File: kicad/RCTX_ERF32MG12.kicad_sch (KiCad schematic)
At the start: 98 parts, among them J20 BUZZER, J21 USB_OTG, P1 SD Card, P2 Nokia 5110 display, Q1 Q_PMOS_DGS, SW1 RESET, U1 PIC16(L)F1459-I_ML

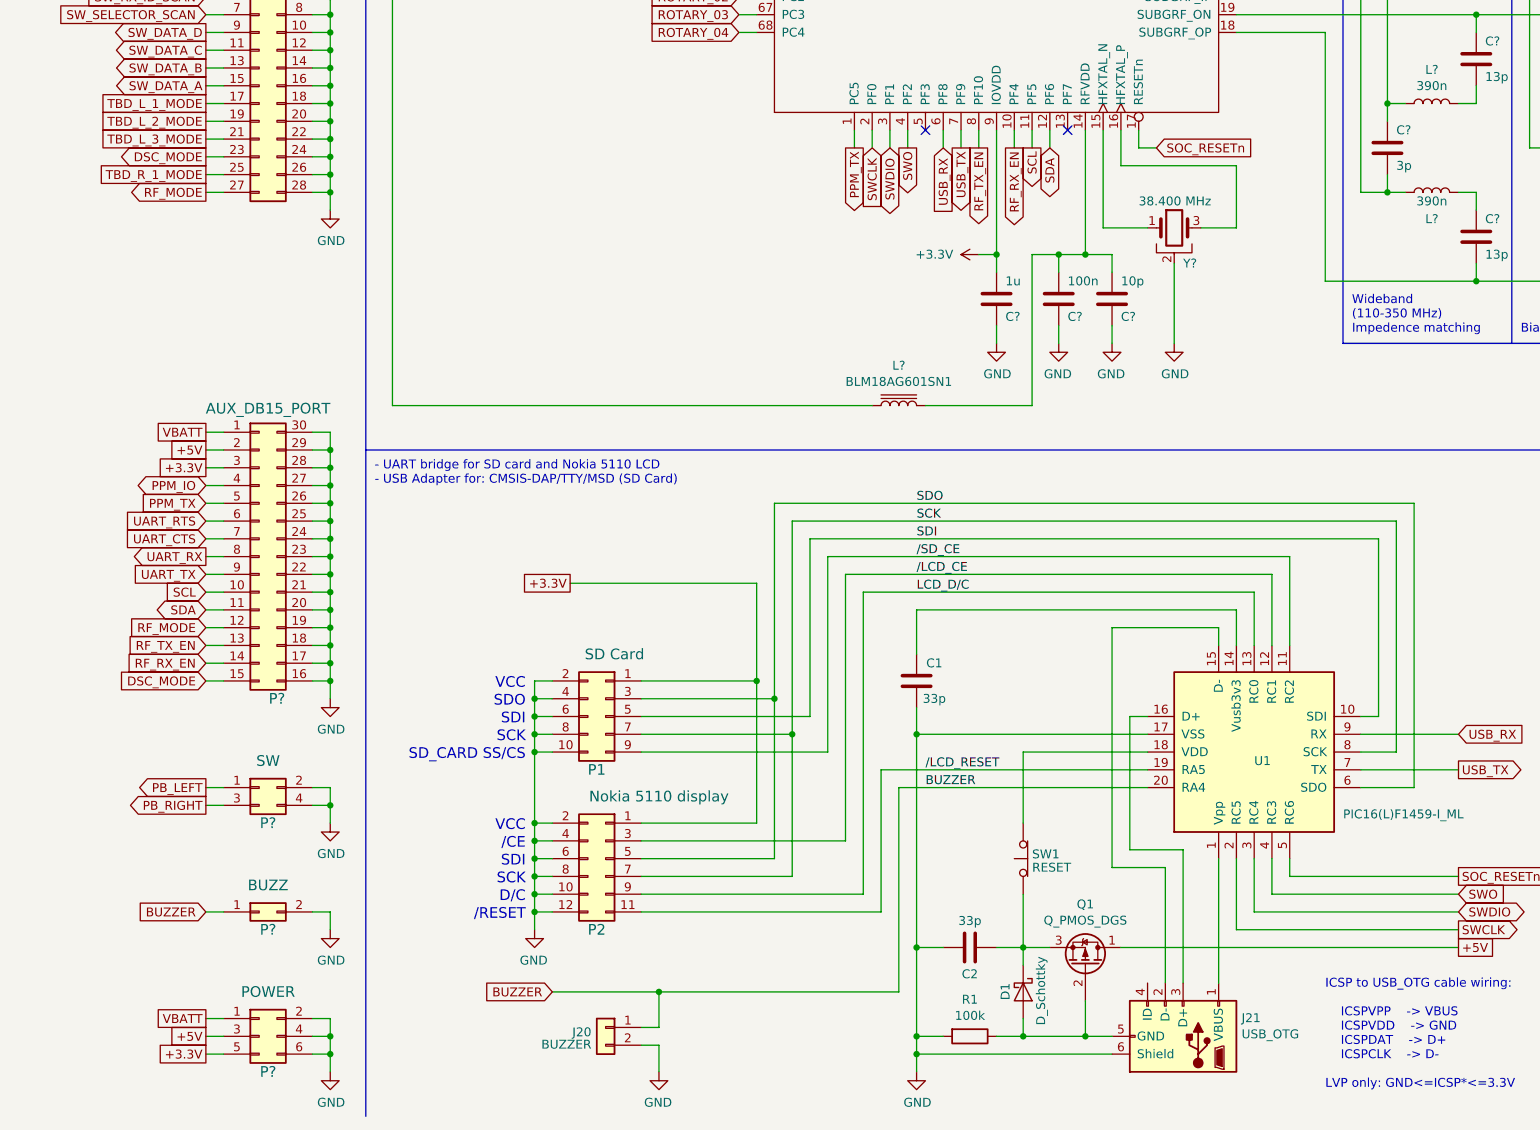
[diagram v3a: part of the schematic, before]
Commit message: Changing the buzzer connector
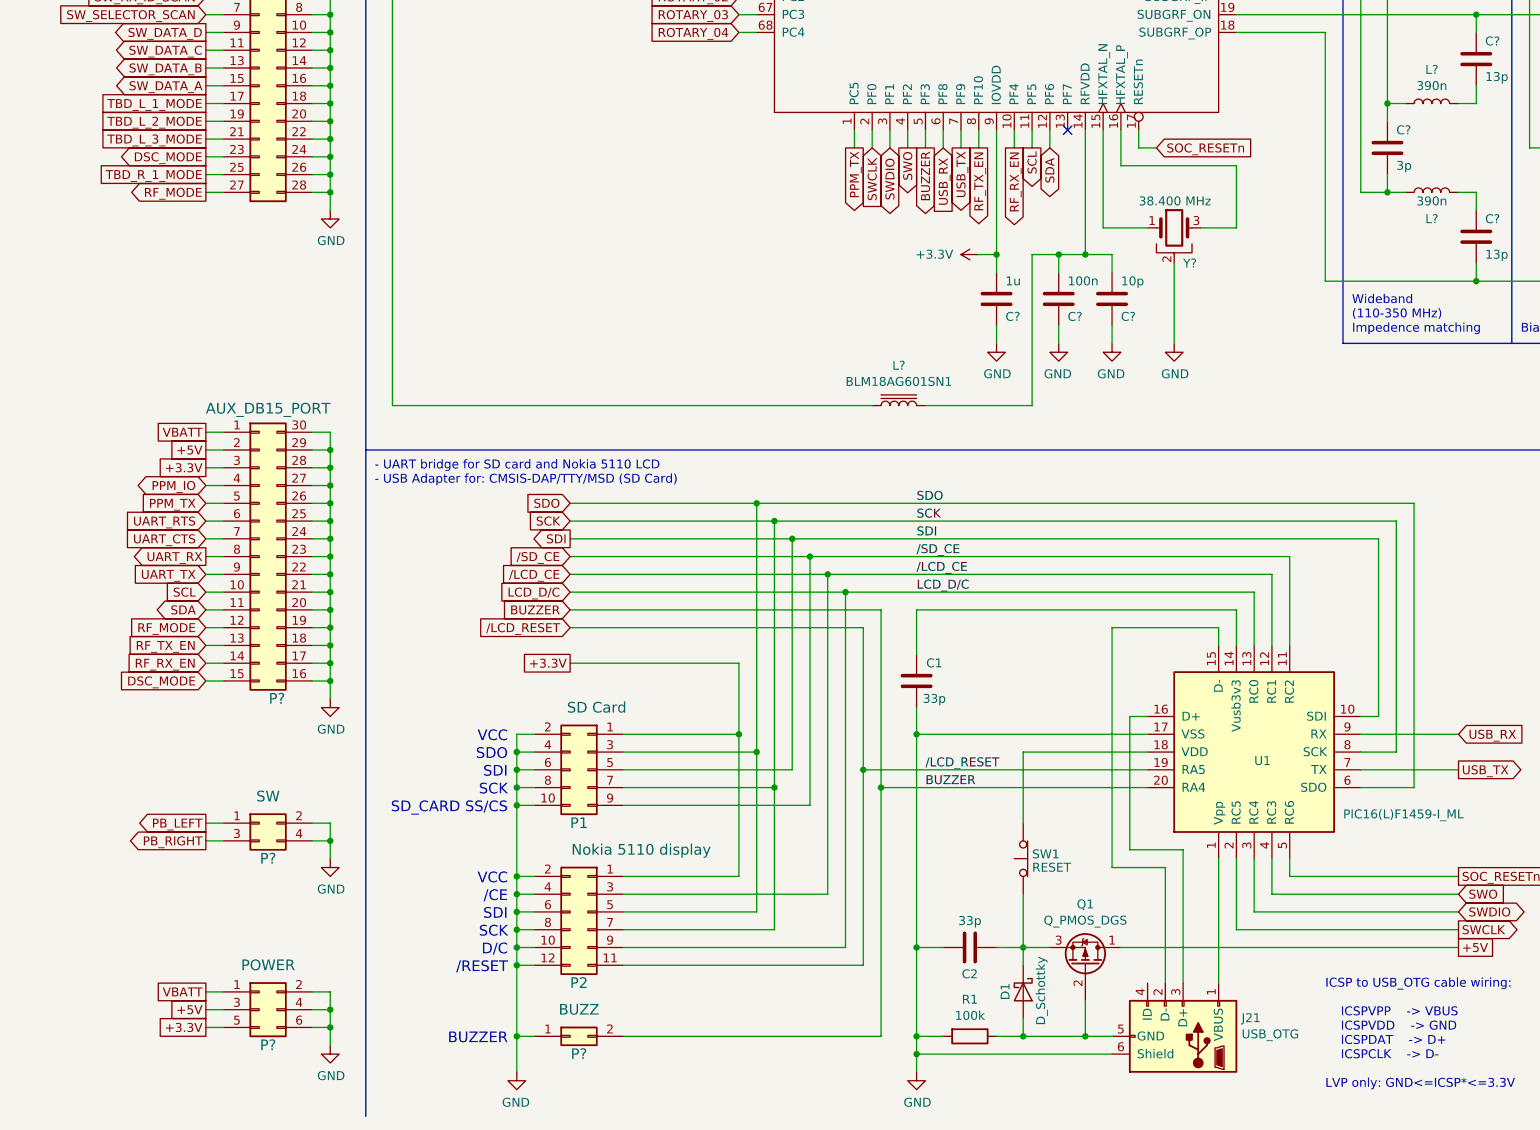
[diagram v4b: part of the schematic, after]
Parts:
- removed J20: BUZZER, symbol Connector_Generic:Conn_01x02
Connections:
- net BUZZER: now also P?.2 (Pin_2), U?.5 (PF3); no longer P?.1 (Pin_1)
- net GND: now also P?.1 (Pin_1); no longer P?.2 (Pin_2)
- no-connect marks 3 -> 2
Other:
- note added: "BUZZER"
- moved on the sheet: P?

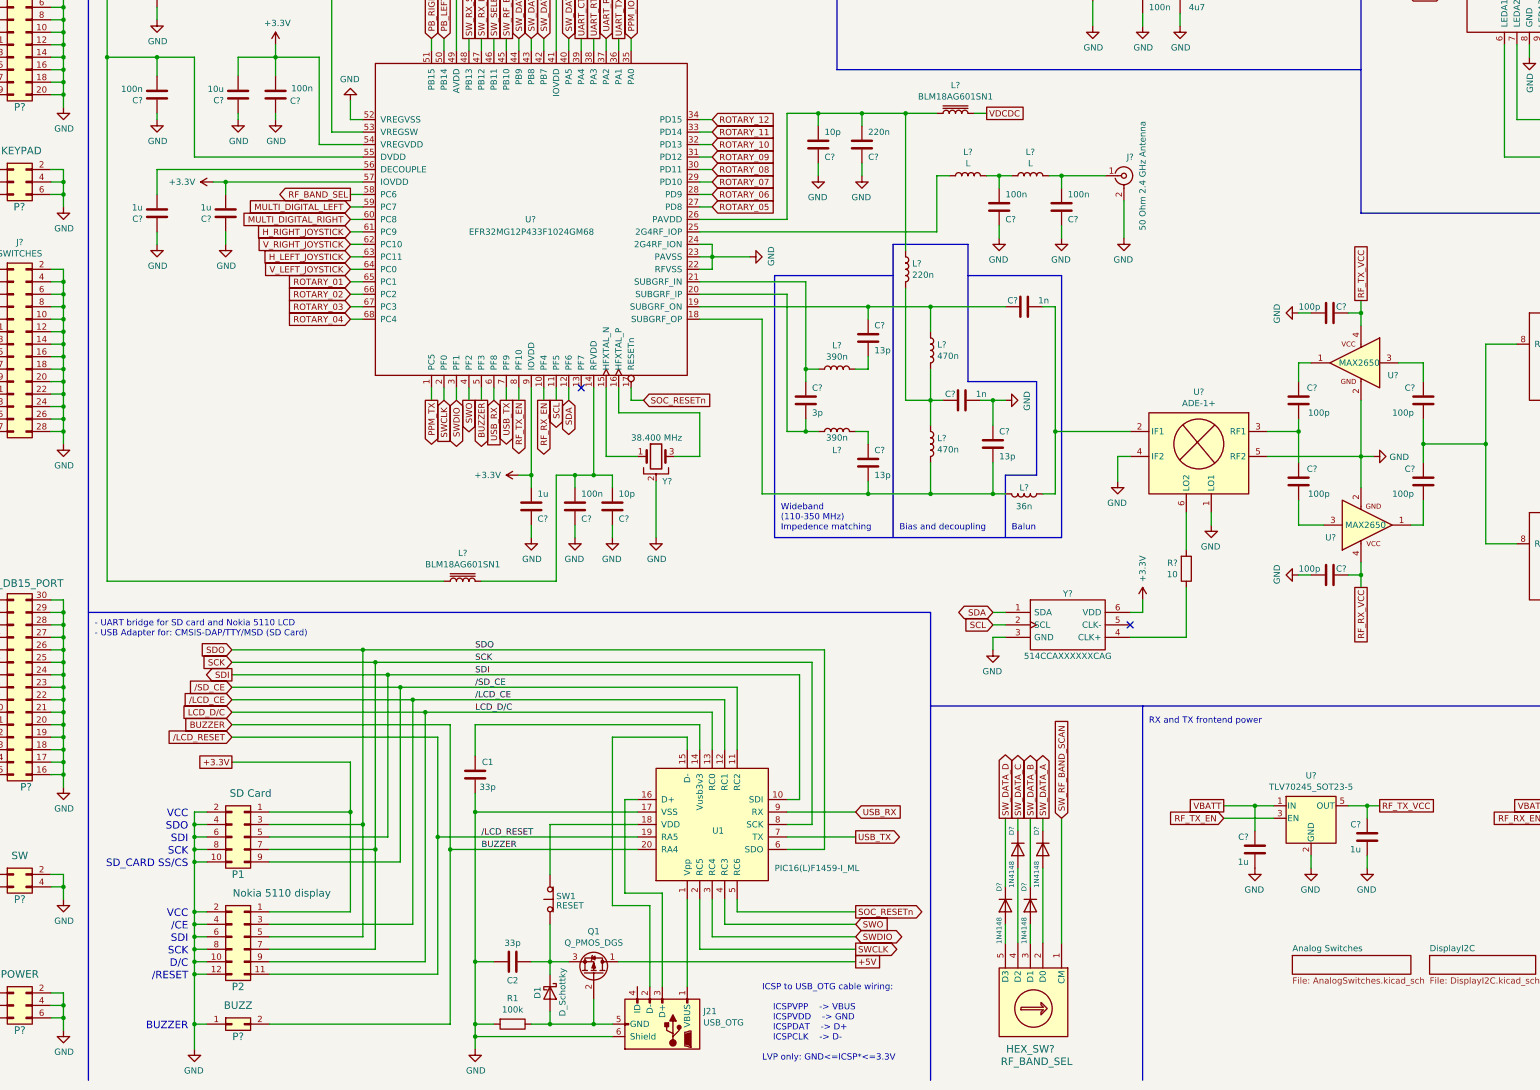
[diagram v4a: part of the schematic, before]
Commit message: Using an930.1-efr32-series-1_2.4GHz-matching-guide.pdf values for 2.4 GHz matching network
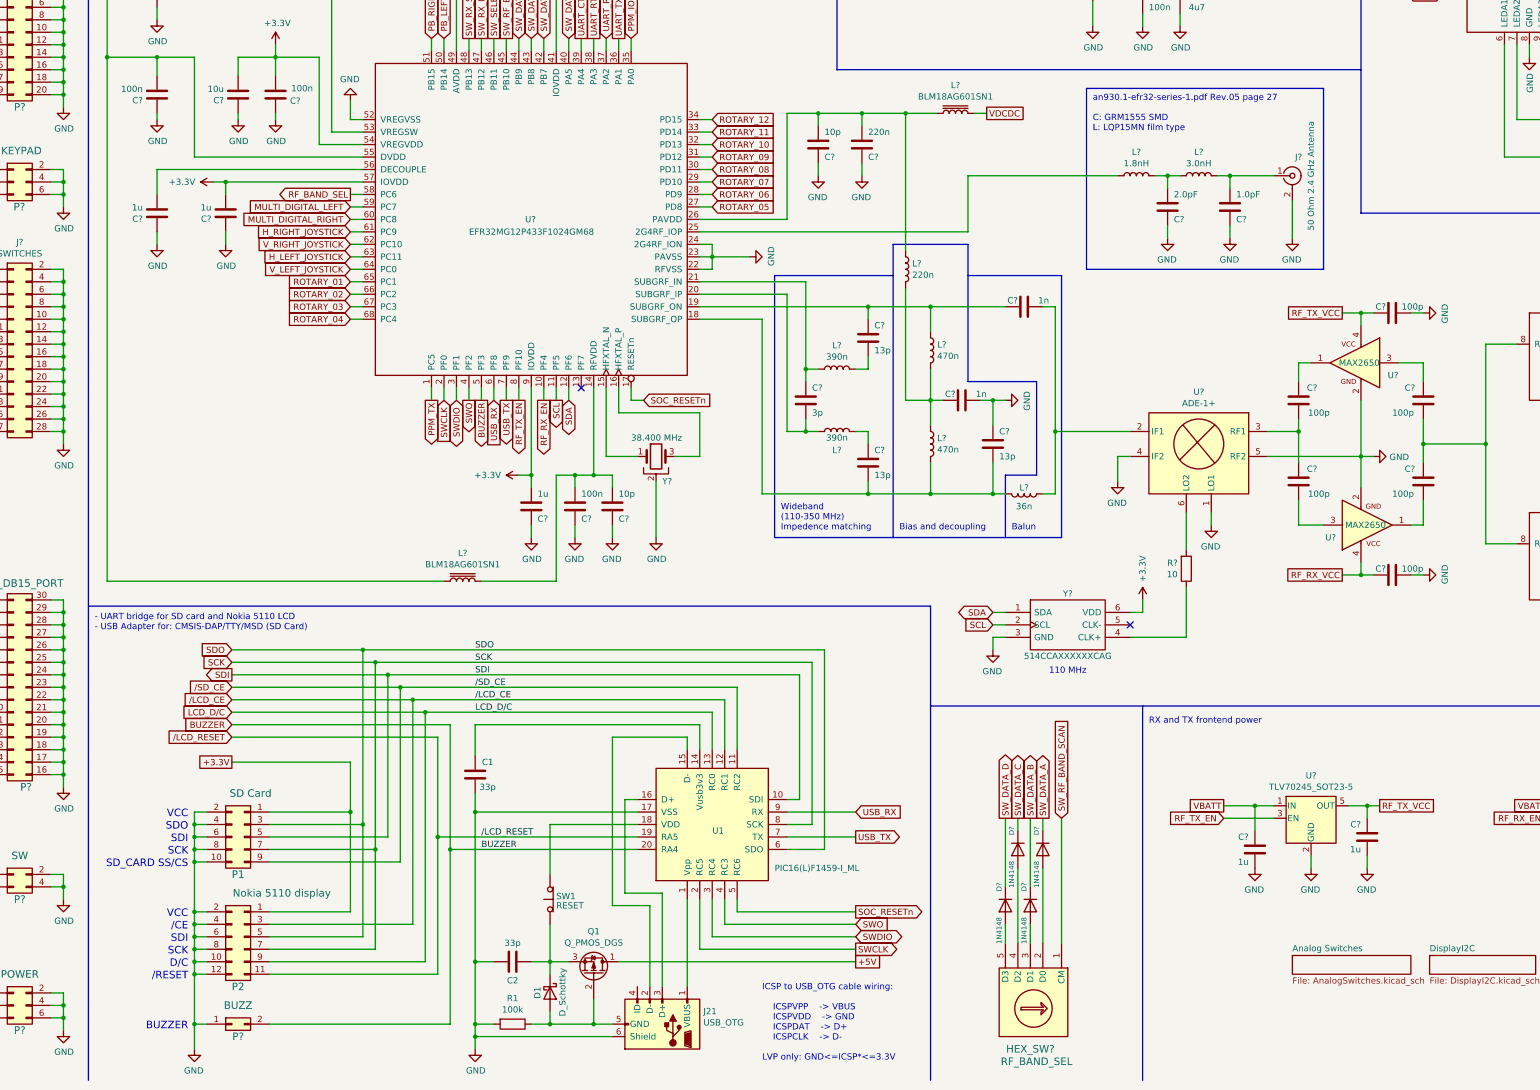
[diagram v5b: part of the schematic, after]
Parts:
- C?: value 100n -> 2.0pF
- C?: value 100n -> 1.0pF
- L?: value L -> 1.8nH
- L?: value L -> 3.0nH
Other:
- note added: "110 MHz"
- note added: "an930.1-efr32-series-1.pdf Rev.05 page 27 C: GRM1555 SMD L: LQP15MN film type"
- moved on the sheet: C?, J?, L?

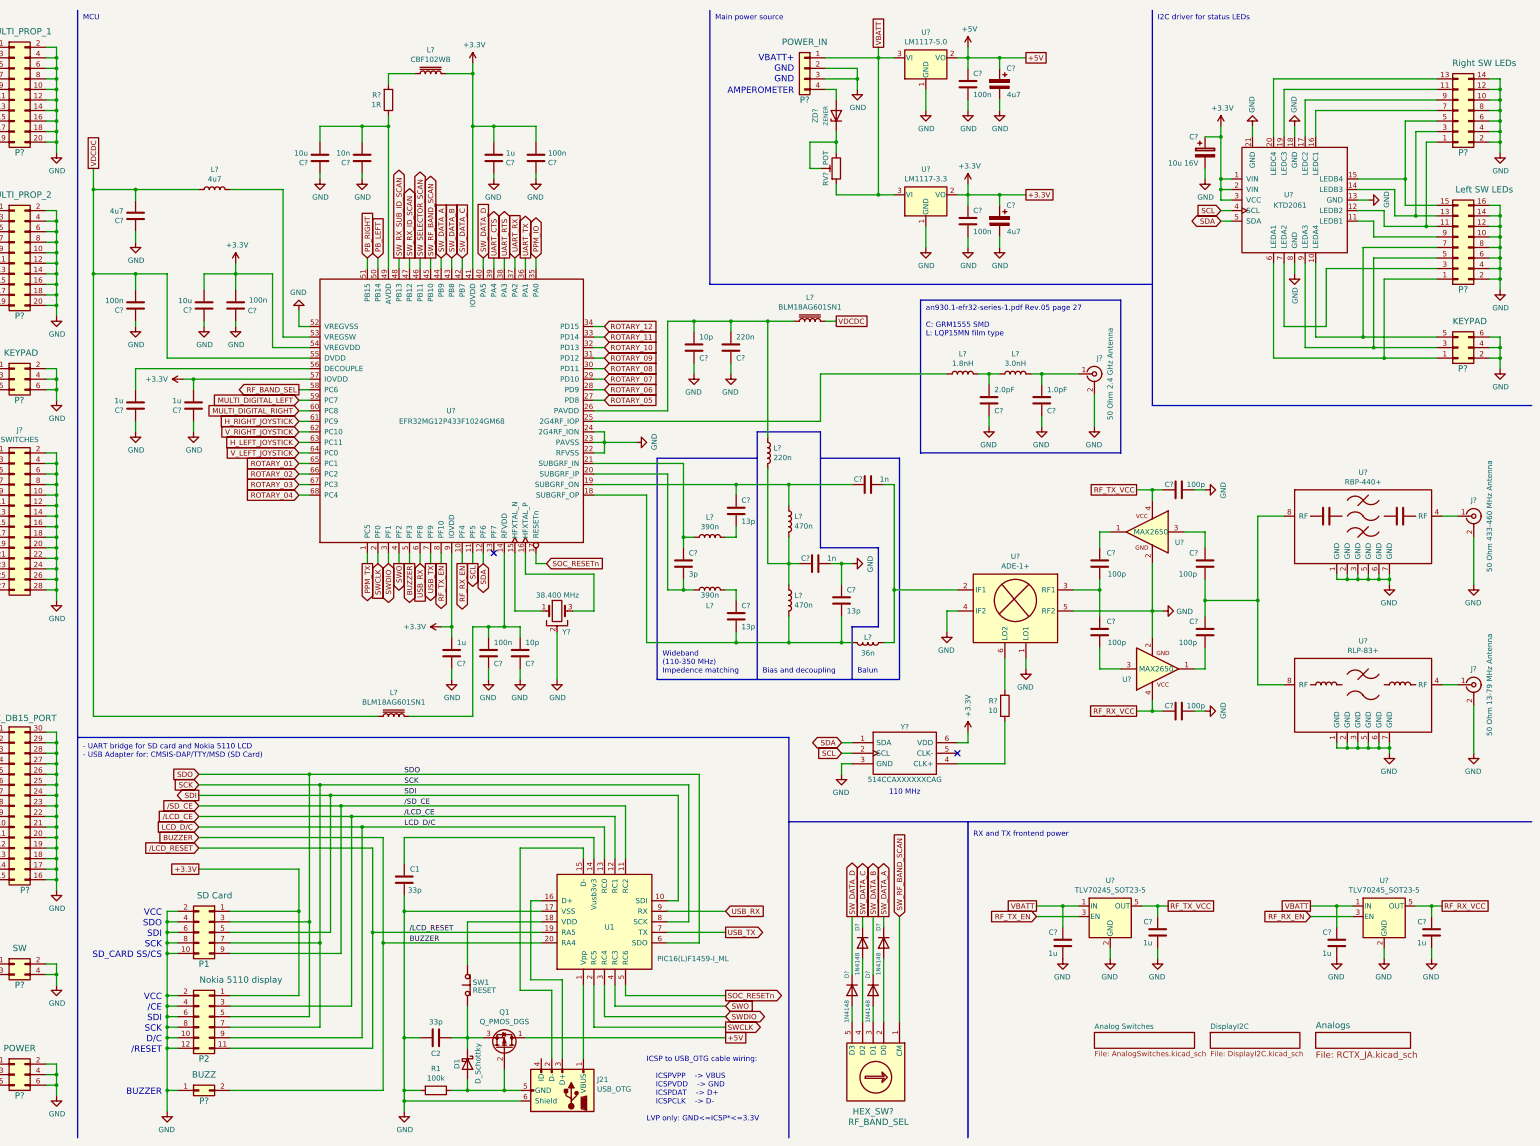
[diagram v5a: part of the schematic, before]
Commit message: Using MAX6969/MAX6971 SPI LEDs driver
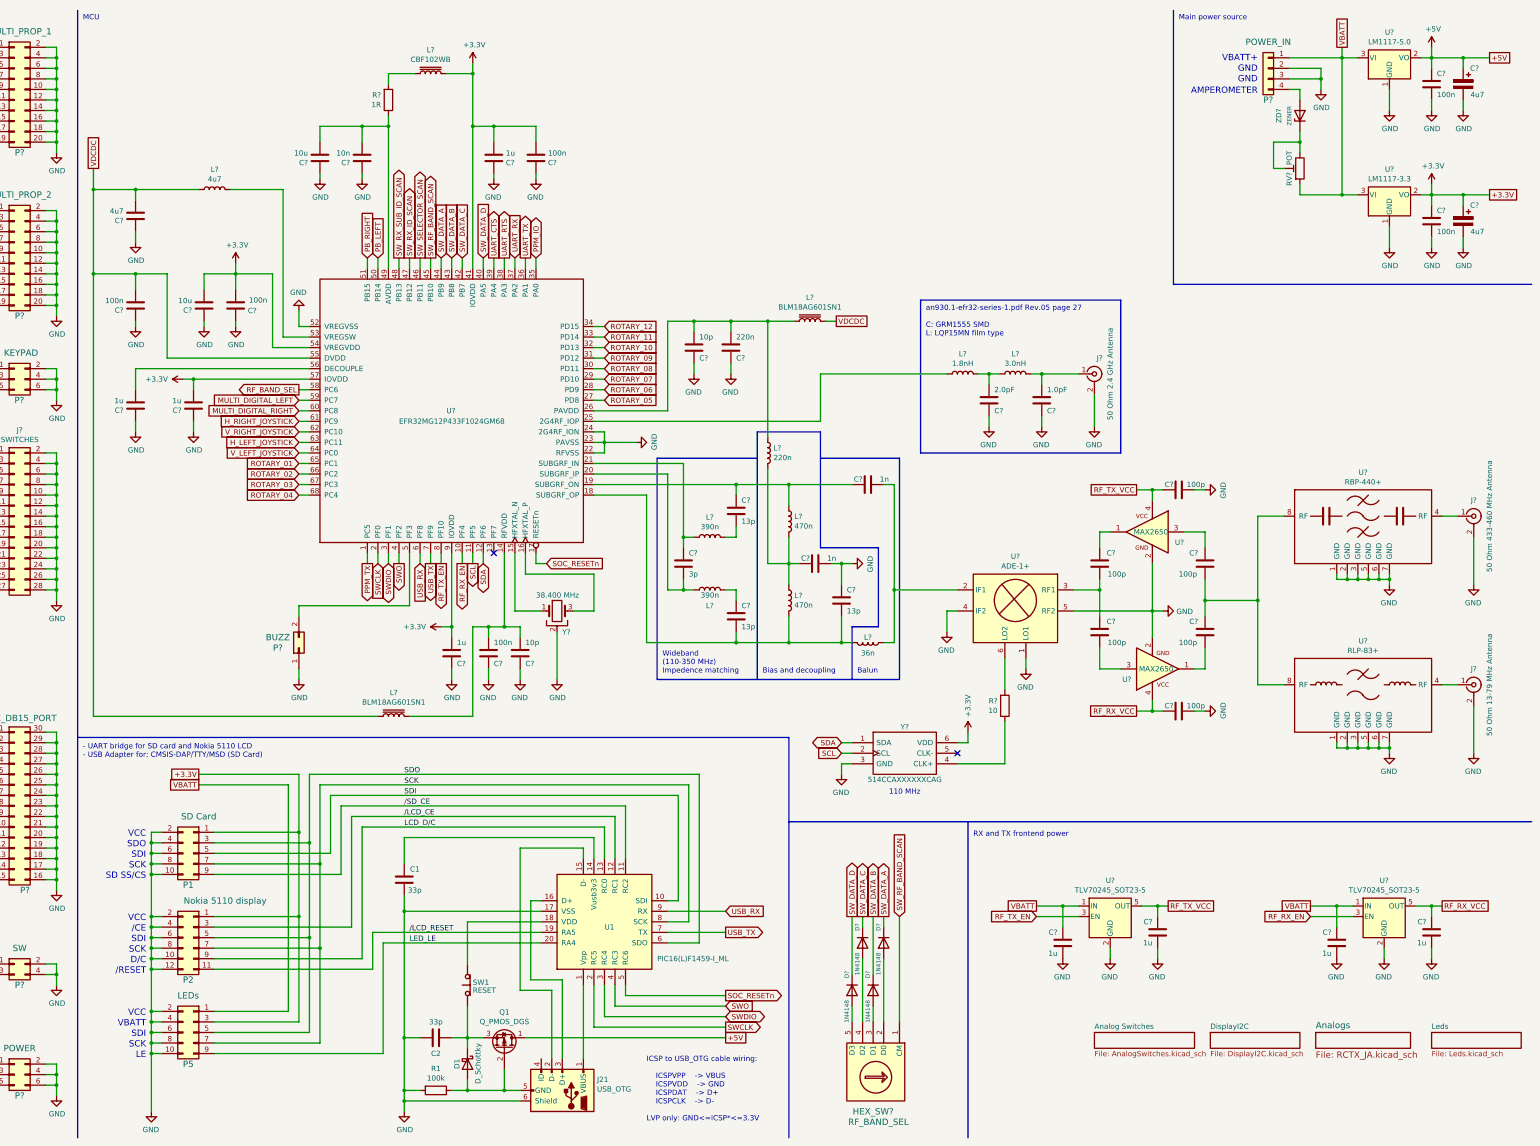
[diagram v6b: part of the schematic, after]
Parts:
- removed C?: 10u 16V, symbol device:CP
- removed P?: KEYPAD, symbol conn:Conn_02x03_Odd_Even
- removed P?: Left SW LEDs, symbol conn:Conn_02x08_Odd_Even
- removed P?: Right SW LEDs, symbol conn:Conn_02x07_Odd_Even
- removed U?: KTD2061, symbol Kinetic:KTD2061
- added P5: LEDs, symbol conn:Conn_02x05_Odd_Even
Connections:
- net +3V3: now also P5.3 (Pin_3)
- net GND: now also P5.10 (Pin_10), P5.2 (Pin_2), P5.4 (Pin_4), P5.6 (Pin_6), P5.8 (Pin_8)
- net SCK: now also P5.7 (Pin_7)
- net SDO: now also P5.5 (Pin_5)
- net VBATT: now also P5.1 (Pin_1)
- net BUZZER: no longer names the net of P?.2 (Pin_2), U?.5 (PF3)
- net BUZZER: no longer U1.20 (RA4)
- new net LED_LE: P5.9 (Pin_9), U1.20 (RA4)
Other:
- added sheet Leds (Leds.kicad_sch)
- note added: "LE"
- note added: "SD SS/CS"
- note added: "VBATT"
- note removed: "BUZZER"
- note removed: "I2C driver for status LEDs"
- note removed: "SD_CARD SS/CS"
- moved on the sheet: C?, P1, P2, P?, RV?, U?, ZD?
